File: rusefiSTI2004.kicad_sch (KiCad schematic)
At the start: 0 parts

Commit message: Low-side drivers Q1-Q20: VND14NV04-E (obsolete) -> onsemi NCV8401BDTRKG
Same DPAK pinout and TO-252-2 footprint; protected (active clamp, current limit, thermal
shutdown), AEC-Q101, about 28 mOhm at 5 V. Netlist unchanged, 0 overlaps. Schematic PDF
regenerated.

Co-Authored-By: Claude Opus 5.5 <noreply@anthropic.com>
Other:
- note added: "Low-side drivers (NCV8401B, protected) in sub-sheets: INJ injectors 1-4; LS1 main relay, fans, ETB relay;"
- note removed: "Low-side drivers (VND14NV04) in sub-sheets: INJ injectors 1-4; LS1 main relay, fans, ETB relay;"
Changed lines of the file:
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@@
 		)
 	)
-	(text "Low-side drivers (VND14NV04) in sub-sheets: INJ\ninjectors 1-4; LS1 main relay, fans, ETB relay;"
+	(text "Low-side drivers (NCV8401B, protected) in sub-sheets: INJ\ninjectors 1-4; LS1 main relay, fans, ETB relay;"
 		(exclude_from_sim no)
 		(at 110.49 156.21 0)

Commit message: Title block: TITLE is the project name (${Project_Name}) on every sheet, DESCRIPTION the sheet name
The LS/INJ sub-sheet and the root had no title at all.

Co-Authored-By: Claude Opus 5.5 <noreply@anthropic.com>
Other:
- title: (none) -> ${Project_Name}
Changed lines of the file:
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@@
 	(paper "A3")
 	(title_block
+		(title "${Project_Name}")
 		(date "2026-10-13")
 	)

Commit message: Low-side drivers sized per load: 8 DPAK (NCV8401B), 4 SOT-223 (ZXMS6006DGQ), 8 SOT-23F (ZXMS6004FF)
INJ and LS2 stay DPAK; LS3 and LS1/LS4 use new sub-sheets with the smaller parts. Purge and the rear
O2 heater swapped groups (LS2/LS3), spares moved to LS3, MIL/tach to LS4; every output keeps its
J1 and MCU pin (checked on the netlist). PCB bank re-placed, planes rebuilt: DRC 0 errors, parity 0.

Co-Authored-By: Claude Opus 5.5 <noreply@anthropic.com>
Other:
- note added: "Protected low-side drivers sized per load (Outputs): 8 DPAK, 4 SOT-223, 8 SOT-23F."
- note removed: "Low-side drivers (NCV8401B, protected) in sub-sheets: INJ injectors 1-4; LS1 main relay, fans, ETB relay;"
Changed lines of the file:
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@@
 		)
 	)
-	(text "Low-side drivers (NCV8401B, protected) in sub-sheets: INJ\ninjectors 1-4; LS1 main relay, fans, ETB relay;"
+	(text "Protected low-side drivers sized per load (Outputs):\n8 DPAK, 4 SOT-223, 8 SOT-23F."
 		(exclude_from_sim no)
 		(at 110.49 156.21 0)

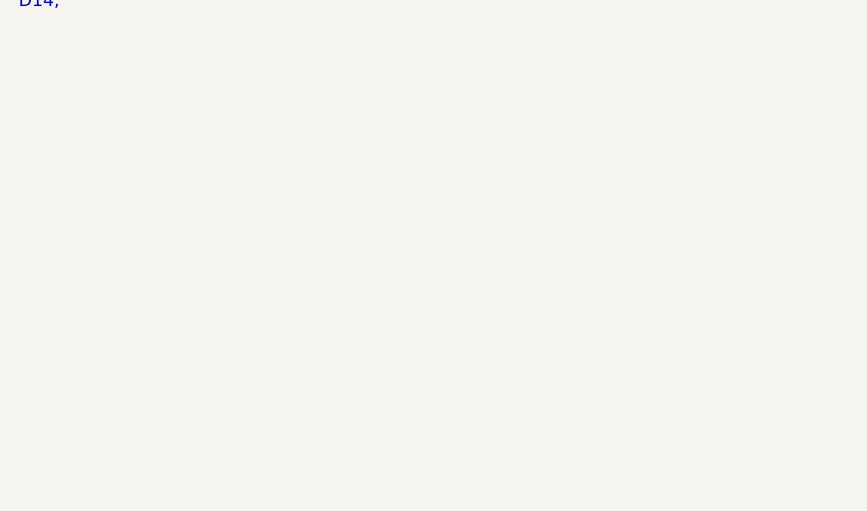
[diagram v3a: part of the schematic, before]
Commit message: On-board MAP sensor (AlphaX style): U20 MPXHZ6400AC6T1 + C1 100n on +5VA -> M1 IN_MAP3 (S19)
TGV position RH moves from IN_MAP3 to IN_RES2 (S14). J3 pin 8 (was AUX_AN1 on
IN_RES2) is now not connected; P28 is the MAP test pad. External MAP stays on
IN_MAP1. PCB: U20/C1 placed left of M1, DRC 0 errors, unconnected 322.

Co-Authored-By: Claude Opus 5.5 <noreply@anthropic.com>
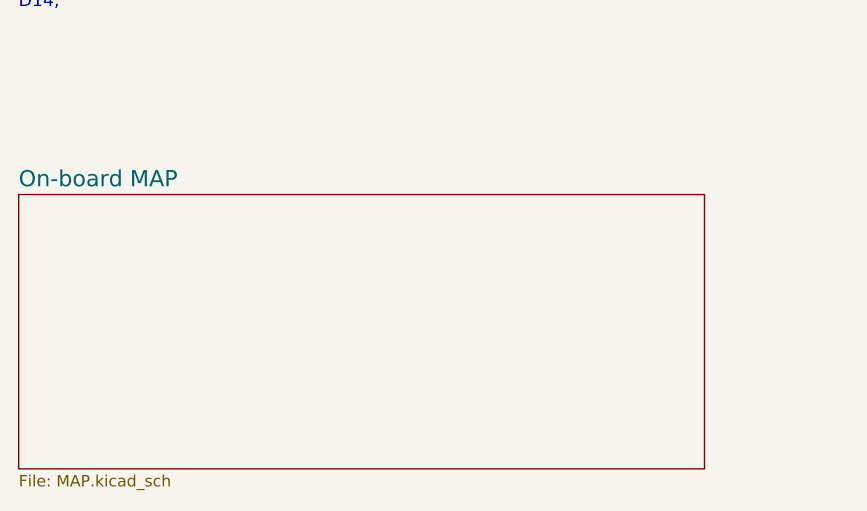
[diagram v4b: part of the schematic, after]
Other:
- added sheet On-board MAP (MAP.kicad_sch)
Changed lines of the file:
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@@
+		)
+	)
+	(sheet
+		(at 15.24 182.88)
+		(size 76.2 30.48)
+		(exclude_from_sim no)
+		(in_bom yes)
+		(on_board yes)
+		(dnp no)
+		(fields_autoplaced yes)
+		(stroke
+			(width 0.1524)
+			(type solid)
+		)
+		(fill
+			(color 0 0 0 0)
+		)
+		(property "Sheetname" "On-board MAP"
+			(at 15.24 182.18 0)
+			(show_name no)
+			(do_not_autoplace no)
+			(effects
+				(font
+					(size 1.8 1.8)
+				)
+				(justify left bottom)
+			)
+		)
+		(property "Sheetfile" "MAP.kicad_sch"
+			(at 15.24 213.98 0)
+			(show_name no)
+			(do_not_autoplace no)
+			(effects
+				(font
+					(size 1.27 1.27)
+				)
+				(justify left top)
+			)
+		)
+		(instances
+			(project "rusefiSTI2004"
+				(path "/00d4d98c-a749-4bd2-a087-ea484becbbe4"
+					(page "15")
+				)
+			)
 		)
 	)

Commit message: On-board MAP: root notes (MAP sheet, fixed stale/truncated notes), IN_MAP_ONBOARD net class pattern + 0.5mm keep-away DRC rule
Rules file probe-checked (5mm probe -> 499 errors). DRC 0 errors, unconnected 322.
Routing plan: move parts instead of necking traces; every net has a rule.

Co-Authored-By: Claude Opus 5.5 <noreply@anthropic.com>
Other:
- note added: "Crank: 2-wire VR sensor (B10 +, B22 -) into M5. Knock (C25) into M13 (the STI has one knock sensor). External MAP (C22) on IN_MAP1."
- note added: "J3: Molex Mini-Fit Jr 2x7 (pinout in documents/README.md): fused 12 V and 5 V, sensor ground, 3 digital in, 1 analog in, 2 low-side, CAN."
- note added: "M11/M12 (dinput4): car lines that close to ground (defogger D11, lights D12, blower D13, test mode D14) and the aux switch inputs."
- note added: "M3: rusEFI wideband (WBO) for a Bosch LSU 4.9 front O2, on CAN to M1. It reaches the sensor through the stock harness (J1 pins 103/104, 126/127/134)."
- note added: "Protected low-side drivers (Outputs): 10 VNLD5160 (SO-8, two channels each) and one NCV8401B DPAK for the rear O2 heater."
- note added: "U20: NXP MPXHZ6400AC6T1 on-board MAP (20-400 kPa abs, top hose port) into M1 IN_MAP3 (S19), as on the rusEFI AlphaX boards."
- note removed: "Crank: 2-wire VR sensor (B10 +, B22 -) into M5. Knock (C25) into M13. M7 is a spare knock channel (not used)."
- note removed: "J3: Molex Mini-Fit Jr 2x7 (pinout in documents/README.md): fused 12 V and 5 V, sensor ground, three digital"
- note removed: "M11/M12 (dinput4): car lines that close to ground (defogger D11, lights D12, blower D13, test mode D14,"
- note removed: "M3: rusEFI wideband (WBO) for a Bosch LSU 4.9 front O2, on CAN to M1. It reaches the sensor through the stock"
- note removed: "Protected low-side drivers sized per load (Outputs): 8 DPAK, 4 SOT-223, 8 SOT-23F."
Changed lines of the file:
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@@
 		)
 	)
-	(text "J3: Molex Mini-Fit Jr 2x7 (pinout in\ndocuments/README.md): fused 12 V and 5 V, sensor\nground, three digital"
+	(text "J3: Molex Mini-Fit Jr 2x7 (pinout in\ndocuments/README.md): fused 12 V and 5 V, sensor\nground, 3 digital in, 1 analog in, 2 low-side, CAN."
 		(exclude_from_sim no)
 		(at 300.99 156.21 0)
@@
 		)
 	)
-	(text "M11/M12 (dinput4): car lines that close to ground\n(defogger D11, lights D12, blower D13, test mode\nD14,"
+	(text "M11/M12 (dinput4): car lines that close to ground\n(defogger D11, lights D12, blower D13, test mode\nD14) and the aux switch inputs."
 		(exclude_from_sim no)
 		(at 15.24 156.21 0)
@@
 		)
 	)
-	(text "M3: rusEFI wideband (WBO) for a Bosch LSU 4.9 front\nO2, on CAN to M1. It reaches the sensor through the\nstock"
+	(text "M3: rusEFI wideband (WBO) for a Bosch LSU 4.9 front\nO2, on CAN to M1. It reaches the sensor through the\nstock harness (J1 pins 103/104, 126/127/134)."
 		(exclude_from_sim no)
 		(at 205.74 156.21 0)
@@
 		)
 	)
-	(text "Crank: 2-wire VR sensor (B10 +, B22 -) into M5.\nKnock (C25) into M13. M7 is a spare knock channel\n(not used)."
+	(text "Crank: 2-wire VR sensor (B10 +, B22 -) into M5.\nKnock (C25) into M13 (the STI has one knock\nsensor). External MAP (C22) on IN_MAP1."
 		(exclude_from_sim no)
 		(at 300.99 95.25 0)
@@
 		)
 	)
-	(text "Protected low-side drivers sized per load (Outputs):\n8 DPAK, 4 SOT-223, 8 SOT-23F."
+	(text "Protected low-side drivers (Outputs): 10 VNLD5160\n(SO-8, two channels each) and one NCV8401B DPAK\nfor the rear O2 heater."
 		(exclude_from_sim no)
 		(at 110.49 156.21 0)
 		(effects
 			(font
+				(size 1.4 1.4)
+			)
+			(justify left top)
+		)
+	)
+	(text "U20: NXP MPXHZ6400AC6T1 on-board MAP (20-400 kPa\nabs, top hose port) into M1 IN_MAP3 (S19), as on\nthe rusEFI AlphaX boards."
+		(exclude_from_sim no)
+		(at 15.24 217.17 0)
+		(effects
+			(font
